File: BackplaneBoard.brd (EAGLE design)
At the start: 139.7 x 76.2 mm, 15 parts

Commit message: fixeey
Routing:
- net +3V3: track 127.7 -> 129.7 mm
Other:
- board text added: "+5V"
- board text added: "CAN"
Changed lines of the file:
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@@
 <?xml version="1.0" encoding="utf-8"?>
 <!DOCTYPE eagle SYSTEM "eagle.dtd">
-<eagle version="9.1.3">
+<eagle version="9.2.0">
 <drawing>
 <settings>
@@
 <wire x1="139.7" y1="76.2" x2="0" y2="76.2" width="0" layer="20"/>
 <wire x1="0" y1="76.2" x2="0" y2="0" width="0" layer="20"/>
+<text x="67.2338" y="71.628" size="1.778" layer="25">CAN</text>
+<text x="56.4134" y="2.1082" size="1.778" layer="25">+5V</text>
 </plain>
 <attributes>
@@
 <vertex x="134.1374" y="48.2346"/>
 <vertex x="134.1374" y="58.0898"/>
-<vertex x="133.9342" y="58.0898"/>
 <vertex x="122.7074" y="58.0898"/>
-<vertex x="122.7074" y="58.0136"/>
 <vertex x="122.7074" y="53.7718"/>
 <vertex x="122.7836" y="53.7718"/>
 <vertex x="120.2182" y="51.2064"/>
-<vertex x="27.3812" y="51.2064"/>
-<vertex x="17.5768" y="61.0108"/>
+<vertex x="25.019" y="51.2064"/>
+<vertex x="15.2146" y="61.0108"/>
 <vertex x="5.5626" y="61.0108"/>
 <vertex x="5.5626" y="50.6984"/>
@@
 <polygon width="0.1524" layer="1">
 <vertex x="35.56" y="20.32"/>
-<vertex x="35.56" y="26.67"/>
-<vertex x="33.02" y="29.21"/>
-<vertex x="27.94" y="29.21"/>
-<vertex x="26.2636" y="30.8864"/>
-<vertex x="26.2636" y="40.7416"/>
-<vertex x="26.2636" y="42.3164"/>
-<vertex x="22.86" y="45.72"/>
+<vertex x="35.56" y="26.3144"/>
+<vertex x="32.5628" y="29.3116"/>
+<vertex x="32.5628" y="41.4274"/>
+<vertex x="28.2702" y="45.72"/>
 <vertex x="21.59" y="45.72"/>
 <vertex x="16.4084" y="50.9016"/>
-<vertex x="16.4084" y="31.3944"/>
-<vertex x="23.5204" y="24.2824"/>
+<vertex x="16.4084" y="29.5656"/>
+<vertex x="23.5204" y="22.4536"/>
 <vertex x="23.5204" y="20.32"/>
+</polygon>
+<polygon width="0.1524" layer="1">
+<vertex x="12.0396" y="60.9854"/>
+<vertex x="24.8666" y="60.9854"/>
+<vertex x="24.8666" y="50.7746"/>
+<vertex x="12.0396" y="50.7746"/>
 </polygon>
 </signal>
@@
 <vertex x="6" y="28"/>
 </polygon>
-<wire x1="38.1" y1="16.51" x2="22.7584" y2="16.51" width="0.8128" layer="1"/>
+<wire x1="38.1" y1="16.51" x2="19.3548" y2="16.51" width="0.8128" layer="1"/>
 <polygon width="0.8128" layer="1">
 <vertex x="115.57" y="20.32"/>
@@
 <vertex x="120.65" y="20.32"/>
 </polygon>
-<wire x1="38.1" y1="16.51" x2="74.93" y2="16.51" width="0.8128" layer="1"/>
+<wire x1="38.1" y1="16.51" x2="76.2" y2="16.51" width="0.8128" layer="1"/>
 <wire x1="78.74" y1="21.59" x2="78.74" y2="19.05" width="0.8128" layer="1"/>
 <wire x1="78.74" y1="19.05" x2="76.2" y2="16.51" width="0.8128" layer="1"/>
-<wire x1="76.2" y1="16.51" x2="74.93" y2="16.51" width="0.8128" layer="1"/>
 <wire x1="40.64" y1="21.59" x2="40.64" y2="19.05" width="0.8128" layer="1"/>
 <wire x1="40.64" y1="19.05" x2="38.1" y2="16.51" width="0.8128" layer="1"/>
@@
 </polygon>
 <wire x1="116.84" y1="19.05" x2="116.84" y2="21.59" width="0.8128" layer="1"/>
-<wire x1="17.0688" y1="22.1996" x2="17.0688" y2="25.908" width="0.8128" layer="1"/>
-<wire x1="17.0688" y1="25.908" x2="13.7668" y2="29.21" width="0.8128" layer="1"/>
+<wire x1="16.0274" y1="26.9494" x2="16.0274" y2="19.8374" width="0.8128" layer="1"/>
+<wire x1="16.0274" y1="26.9494" x2="13.7668" y2="29.21" width="0.8128" layer="1"/>
 <wire x1="13.7668" y1="29.21" x2="12.4" y2="29.21" width="0.8128" layer="1"/>
-<wire x1="22.7584" y1="16.51" x2="17.0688" y2="22.1996" width="0.8128" layer="1"/>
+<wire x1="19.3548" y1="16.51" x2="16.0274" y2="19.8374" width="0.8128" layer="1"/>
 </signal>
 <signal name="CAN_H">

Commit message: Version #3
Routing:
- net CAN_L: track 286.2 -> 223.3 mm
- net CAN_H: track 183.3 -> 215.6 mm
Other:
- board text added: "+12V"
- board text added: "GND"

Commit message: Version 4
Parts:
- added U$12, U$13: T2I, BackplaneParts:T2I
- moved U$8 4.93 mm to (44.1, 5.92)
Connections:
- net +5V: now also U$12.1, U$12.2, U$12.3, U$12.4
- net GND: now also U$13.1, U$13.2, U$13.3, U$13.4
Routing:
- net +5V: track 97.9 -> 91.9 mm
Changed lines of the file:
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@@
 <wire x1="0" y1="76.2" x2="0" y2="0" width="0" layer="20"/>
 <text x="67.2338" y="71.628" size="1.778" layer="25">CAN</text>
-<text x="56.4134" y="2.1082" size="1.778" layer="25">+5V</text>
+<text x="51.7652" y="1.8796" size="1.778" layer="25">+5V</text>
 <text x="7.8232" y="62.5094" size="1.778" layer="25">+12V</text>
 <text x="7.493" y="12.065" size="1.778" layer="25">GND</text>
@@
 <text x="63.8048" y="44.2214" size="1.778" layer="25">+12V</text>
 <text x="25.5778" y="18.0086" size="1.778" layer="25">+12V</text>
+<text x="71.9582" y="2.286" size="1.778" layer="25">+5V</text>
+<text x="91.7194" y="2.413" size="1.778" layer="25">GND</text>
 </plain>
 <attributes>
@@
 <element name="U$6" library="BackplaneParts" package="T2I" value="T2I" x="45" y="42"/>
 <element name="U$7" library="BackplaneParts" package="T2I" value="T2I" x="87.988" y="70.636" rot="R180"/>
-<element name="U$8" library="BackplaneParts" package="T2I" value="T2I" x="49" y="6"/>
+<element name="U$8" library="BackplaneParts" package="T2I" value="T2I" x="44.0724" y="5.9238"/>
 <element name="U$9" library="BackplaneParts" package="T2I" value="T2I" x="27" y="42"/>
 <element name="U$10" library="BackplaneParts" package="T2I" value="T2I" x="45" y="31"/>
 <element name="U$11" library="BackplaneParts" package="T2I" value="T2I" x="27" y="31"/>
+<element name="U$12" library="BackplaneParts" package="T2I" value="T2I" x="63.754" y="5.8674"/>
+<element name="U$13" library="BackplaneParts" package="T2I" value="T2I" x="83.5406" y="6.1468"/>
 </elements>
 <signals>
@@
 <vertex x="139.7" y="76.2"/>
 </polygon>
+<contactref element="U$13" pad="1"/>
+<contactref element="U$13" pad="2"/>
+<contactref element="U$13" pad="3"/>
+<contactref element="U$13" pad="4"/>
 </signal>
 <signal name="+12V">
@@
 <contactref element="U$9" pad="1"/>
 <polygon width="0.2" layer="1">
-<vertex x="46" y="58"/>
-<vertex x="58" y="58"/>
+<vertex x="45.873" y="58.2794"/>
+<vertex x="58" y="58.2794"/>
 <vertex x="58" y="41"/>
-<vertex x="46" y="41"/>
+<vertex x="45.873" y="41"/>
 </polygon>
 <polygon width="0.1524" layer="1">
@@
 <vertex x="126.5428" y="40.64"/>
 <vertex x="134.1374" y="48.2346"/>
-<vertex x="134.1374" y="58.0898"/>
-<vertex x="122.7074" y="58.0898"/>
-<vertex x="122.7074" y="53.7718"/>
+<vertex x="134.1374" y="58.2676"/>
+<vertex x="122.3772" y="58.2676"/>
+<vertex x="122.3772" y="53.7718"/>
 <vertex x="122.7836" y="53.7718"/>
 <vertex x="120.2182" y="51.2064"/>
@@
 <contactref element="U$4" pad="P$G"/>
 <contactref element="U$4" pad="P$H"/>
+<polygon width="0.1524" layer="1">
+<vertex x="6" y="29"/>
+<vertex x="6" y="37"/>
+<vertex x="11" y="37"/>
+<vertex x="11" y="35"/>
+<vertex x="14" y="35"/>
+<vertex x="14" y="28"/>
+<vertex x="6" y="28"/>
+</polygon>
+<wire x1="38.1" y1="16.51" x2="19.3548" y2="16.51" width="0.8128" layer="1"/>
+<polygon width="0.8128" layer="1">
+<vertex x="115.57" y="20.32"/>
+<vertex x="115.57" y="25.4"/>
+<vertex x="120.65" y="20.32"/>
+</polygon>
+<wire x1="38.1" y1="16.51" x2="76.2" y2="16.51" width="0.8128" layer="1"/>
+<wire x1="78.74" y1="21.59" x2="78.74" y2="19.05" width="0.8128" layer="1"/>
+<wire x1="78.74" y1="19.05" x2="76.2" y2="16.51" width="0.8128" layer="1"/>
+<wire x1="40.64" y1="21.59" x2="40.64" y2="19.05" width="0.8128" layer="1"/>
+<wire x1="40.64" y1="19.05" x2="38.1" y2="16.51" width="0.8128" layer="1"/>
+<wire x1="76.2" y1="16.51" x2="114.3" y2="16.51" width="0.8128" layer="1"/>
+<wire x1="114.3" y1="16.51" x2="116.84" y2="19.05" width="0.8128" layer="1"/>
+<polygon width="0.1524" layer="1">
+<vertex x="39.37" y="20.32"/>
+<vertex x="39.37" y="25.4"/>
+<vertex x="44.45" y="25.4"/>
+<vertex x="44.45" y="20.32"/>
+</polygon>
+<polygon width="0.1524" layer="1">
+<vertex x="77.47" y="20.32"/>
+<vertex x="77.47" y="25.4"/>
+<vertex x="82.55" y="25.4"/>
+<vertex x="82.55" y="20.32"/>
+</polygon>
+<polygon width="0.1524" layer="1">
+<vertex x="115.57" y="20.32"/>
+<vertex x="115.57" y="25.4"/>
+<vertex x="120.65" y="25.4"/>
+<vertex x="120.65" y="20.32"/>
+</polygon>
+<wire x1="116.84" y1="19.05" x2="116.84" y2="21.59" width="0.8128" layer="1"/>
+<wire x1="16.0274" y1="19.8374" x2="16.0274" y2="26.9494" width="0.8128" layer="1"/>
+<wire x1="19.3548" y1="16.51" x2="16.0274" y2="19.8374" width="0.8128" layer="1"/>
+<contactref element="U$1" pad="17"/>
+<contactref element="U$1" pad="18"/>
+<contactref element="U$1" pad="19"/>
 <contactref element="U$1" pad="1"/>
 <contactref element="U$1" pad="4"/>
@@
 <contactref element="U$1" pad="11"/>
 <contactref element="U$1" pad="12"/>
-<contactref element="U$1" pad="17"/>
-<contactref element="U$1" pad="18"/>
-<contactref element="U$1" pad="19"/>
-<polygon width="0.1524" layer="1">
-<vertex x="6" y="29"/>
-<vertex x="6" y="37"/>
-<vertex x="11" y="37"/>
-<vertex x="11" y="35"/>
-<vertex x="14" y="35"/>
-<vertex x="14" y="28"/>
-<vertex x="6" y="28"/>
-</polygon>
-<wire x1="38.1" y1="16.51" x2="19.3548" y2="16.51" width="0.8128" layer="1"/>
-<polygon width="0.8128" layer="1">
-<vertex x="115.57" y="20.32"/>
-<vertex x="115.57" y="25.4"/>
-<vertex x="120.65" y="20.32"/>
-</polygon>
-<wire x1="38.1" y1="16.51" x2="76.2" y2="16.51" width="0.8128" layer="1"/>
-<wire x1="78.74" y1="21.59" x2="78.74" y2="19.05" width="0.8128" layer="1"/>
-<wire x1="78.74" y1="19.05" x2="76.2" y2="16.51" width="0.8128" layer="1"/>
-<wire x1="40.64" y1="21.59" x2="40.64" y2="19.05" width="0.8128" layer="1"/>
-<wire x1="40.64" y1="19.05" x2="38.1" y2="16.51" width="0.8128" layer="1"/>
-<wire x1="76.2" y1="16.51" x2="114.3" y2="16.51" width="0.8128" layer="1"/>
-<wire x1="114.3" y1="16.51" x2="116.84" y2="19.05" width="0.8128" layer="1"/>
-<polygon width="0.1524" layer="1">
-<vertex x="39.37" y="20.32"/>
-<vertex x="39.37" y="25.4"/>
-<vertex x="44.45" y="25.4"/>
-<vertex x="44.45" y="20.32"/>
-</polygon>
-<polygon width="0.1524" layer="1">
-<vertex x="77.47" y="20.32"/>
-<vertex x="77.47" y="25.4"/>
-<vertex x="82.55" y="25.4"/>
-<vertex x="82.55" y="20.32"/>
-</polygon>
-<polygon width="0.1524" layer="1">
-<vertex x="115.57" y="20.32"/>
-<vertex x="115.57" y="25.4"/>
-<vertex x="120.65" y="25.4"/>
-<vertex x="120.65" y="20.32"/>
-</polygon>
-<wire x1="116.84" y1="19.05" x2="116.84" y2="21.59" width="0.8128" layer="1"/>
-<wire x1="16.0274" y1="26.9494" x2="16.0274" y2="19.8374" width="0.8128" layer="1"/>
 <wire x1="16.0274" y1="26.9494" x2="13.7668" y2="29.21" width="0.8128" layer="1"/>
 <wire x1="13.7668" y1="29.21" x2="12.4" y2="29.21" width="0.8128" layer="1"/>
-<wire x1="19.3548" y1="16.51" x2="16.0274" y2="19.8374" width="0.8128" layer="1"/>
 </signal>
 <signal name="CAN_H">
@@
 </signal>
 <signal name="+5V">
-<contactref element="U$1" pad="13"/>
-<contactref element="U$1" pad="15"/>
-<contactref element="U$1" pad="16"/>
-<contactref element="U$1" pad="14"/>
+<contactref element="U$8" pad="4"/>
+<contactref element="U$8" pad="3"/>
+<contactref element="U$8" pad="2"/>
+<contactref element="U$8" pad="1"/>
+<polygon width="1.016" layer="1">
+<vertex x="43.3612" y="12"/>
+<vertex x="43.3612" y="5"/>
+<vertex x="82.1384" y="5"/>
+<vertex x="82.1384" y="12"/>
+</polygon>
+<wire x1="2" y1="10" x2="2" y2="39.13" width="1.27" layer="1"/>
+<wire x1="2" y1="10" x2="10" y2="2" width="1.27" layer="1"/>
+<polygon width="0.1524" layer="1">
+<vertex x="6.35" y="48.26"/>
+<vertex x="12.7" y="48.26"/>
+<vertex x="12.7" y="40.64"/>
+<vertex x="11.43" y="40.64"/>
+<vertex x="11.43" y="38.1"/>
+<vertex x="6.35" y="38.1"/>
+</polygon>
 <contactref element="U$1" pad="22"/>
 <contactref element="U$1" pad="23"/>
@@
 <contactref element="U$1" pad="7"/>
 <contactref element="U$1" pad="6"/>
-<contactref element="U$8" pad="4"/>
-<contactref element="U$8" pad="3"/>
-<contactref element="U$8" pad="2"/>
-<contactref element="U$8" pad="1"/>
-<polygon width="1.016" layer="1">
-<vertex x="49" y="12"/>
-<vertex x="49" y="5"/>
-<vertex x="67" y="5"/>
-<vertex x="67" y="12"/>
-</polygon>
-<wire x1="7.32" y1="44.45" x2="2" y2="39.13" width="1.27" layer="1"/>
-<wire x1="2" y1="39.13" x2="2" y2="10" width="1.27" layer="1"/>
-<wire x1="2" y1="10" x2="10" y2="2" width="1.27" layer="1"/>
-<wire x1="10" y1="2" x2="50" y2="2" width="1.27" layer="1"/>
-<wire x1="50" y1="2" x2="56.8" y2="8.8" width="1.27" layer="1"/>
-<wire x1="56.8" y1="8.8" x2="57.1" y2="8.8" width="1.27" layer="1"/>
-<polygon width="0.1524" layer="1">
-<vertex x="6.35" y="48.26"/>
-<vertex x="12.7" y="48.26"/>
-<vertex x="12.7" y="40.64"/>
-<vertex x="11.43" y="40.64"/>
-<vertex x="11.43" y="38.1"/>
-<vertex x="6.35" y="38.1"/>
-</polygon>
+<contactref element="U$1" pad="13"/>
+<contactref element="U$1" pad="15"/>
+<contactref element="U$1" pad="16"/>
+<contactref element="U$1" pad="14"/>
+<contactref element="U$12" pad="4"/>
+<contactref element="U$12" pad="3"/>
+<contactref element="U$12" pad="2"/>
+<contactref element="U$12" pad="1"/>
+<wire x1="10" y1="2" x2="45.4486" y2="2" width="1.27" layer="1"/>
+<wire x1="45.4486" y1="2" x2="52.1724" y2="8.7238" width="1.27" layer="1"/>
+<wire x1="2" y1="39.13" x2="2" y2="39.13" width="1.27" layer="1"/>
+<wire x1="2" y1="39.13" x2="4.78" y2="41.91" width="1.27" layer="1"/>
+<wire x1="4.78" y1="41.91" x2="7.32" y2="41.91" width="1.27" layer="1"/>
 </signal>
 </signals>

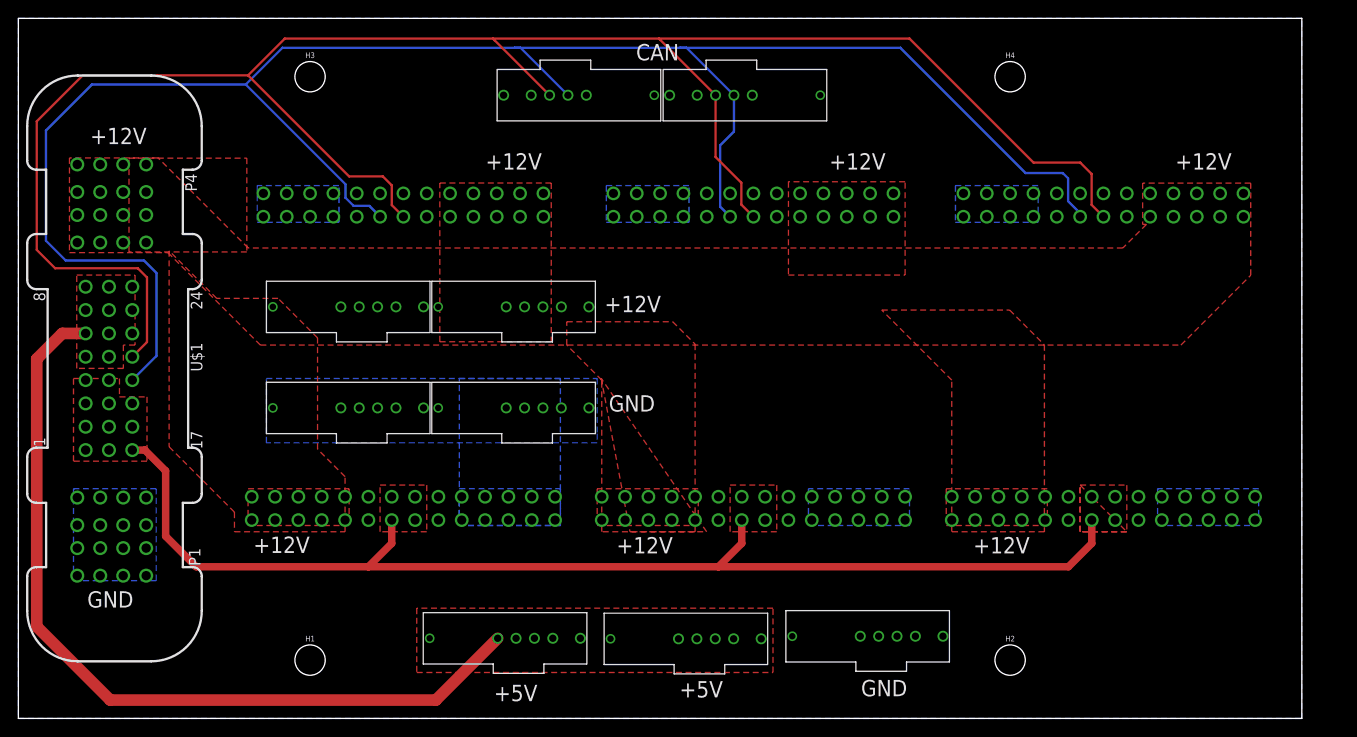
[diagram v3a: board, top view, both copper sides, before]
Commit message: edited GND plane
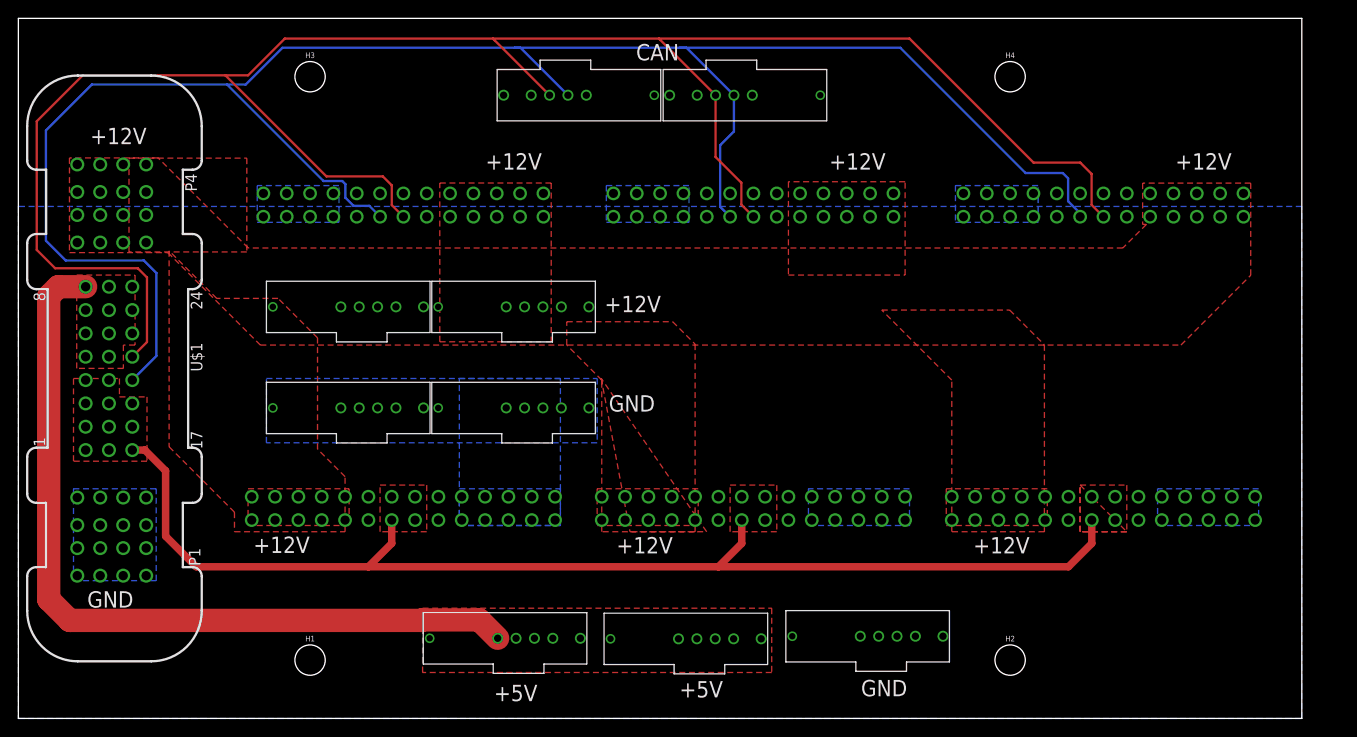
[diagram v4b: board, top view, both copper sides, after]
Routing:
- net CAN_L: track 223.3 -> 225.8 mm
- net CAN_H: track 215.6 -> 217.6 mm
- net +5V: track 91.9 -> 91.3 mm
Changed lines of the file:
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@@
 </polygon>
 <polygon width="0.8128" layer="16">
-<vertex x="0" y="76.2"/>
+<vertex x="0" y="55.7276"/>
 <vertex x="0" y="0"/>
 <vertex x="139.7" y="0"/>
-<vertex x="139.7" y="76.2"/>
+<vertex x="139.7" y="55.7276"/>
 </polygon>
 <contactref element="U$13" pad="1"/>
@@
 <wire x1="3" y1="52" x2="3" y2="64" width="0.254" layer="16"/>
 <wire x1="3" y1="64" x2="8" y2="69" width="0.254" layer="16"/>
-<wire x1="8" y1="69" x2="24.7498" y2="69" width="0.254" layer="16"/>
-<wire x1="24.7498" y1="69" x2="35.5974" y2="58.1524" width="0.254" layer="16"/>
+<wire x1="8" y1="69" x2="22.7076" y2="69" width="0.254" layer="16"/>
+<wire x1="22.7076" y1="69" x2="24.7498" y2="69" width="0.254" layer="16"/>
 <wire x1="35.5974" y1="58.1524" x2="35.5974" y2="56.6771625" width="0.254" layer="16"/>
 <wire x1="35.5974" y1="56.6771625" x2="36.4777625" y2="55.7968" width="0.254" layer="16"/>
@@
 <wire x1="24.7498" y1="69" x2="28.7498" y2="73" width="0.254" layer="16"/>
 <wire x1="28.7498" y1="73" x2="54" y2="73" width="0.254" layer="16"/>
+<wire x1="22.7076" y1="69" x2="33.2114" y2="58.4962" width="0.254" layer="16"/>
+<wire x1="35.2536" y1="58.4962" x2="35.5974" y2="58.1524" width="0.254" layer="16"/>
+<wire x1="33.2114" y1="58.4962" x2="35.2536" y2="58.4962" width="0.254" layer="16"/>
 </signal>
 <signal name="CAN_L">
@@
 <wire x1="51.656" y1="74" x2="51.828" y2="73.828" width="0.254" layer="1"/>
 <wire x1="51.828" y1="73.828" x2="57.82" y2="67.836" width="0.254" layer="1"/>
-<wire x1="7" y1="70" x2="25" y2="70" width="0.254" layer="1"/>
+<wire x1="7" y1="70" x2="22.5298" y2="70" width="0.254" layer="1"/>
+<wire x1="22.5298" y1="70" x2="25" y2="70" width="0.254" layer="1"/>
 <wire x1="51.656" y1="74" x2="69.724" y2="74" width="0.254" layer="1"/>
 <wire x1="69.724" y1="74" x2="69.862" y2="73.862" width="0.254" layer="1"/>
@@
 <wire x1="78.6952" y1="55.9248" x2="80.01" y2="54.61" width="0.254" layer="1"/>
 <wire x1="75.888" y1="61.112" x2="78.6952" y2="58.3048" width="0.254" layer="1"/>
-<wire x1="25" y1="70" x2="36" y2="59" width="0.254" layer="1"/>
-<wire x1="36" y1="59" x2="39.6698" y2="59" width="0.254" layer="1"/>
 <wire x1="39.6698" y1="59" x2="40.6444" y2="58.0254" width="0.254" layer="1"/>
 <wire x1="40.6444" y1="55.8756" x2="41.91" y2="54.61" width="0.254" layer="1"/>
 <wire x1="40.6444" y1="58.0254" x2="40.6444" y2="55.8756" width="0.254" layer="1"/>
+<wire x1="22.5298" y1="70" x2="33.5298" y2="59" width="0.254" layer="1"/>
+<wire x1="33.5298" y1="59" x2="39.6698" y2="59" width="0.254" layer="1"/>
 </signal>
 <signal name="+5V">
@@
 <contactref element="U$8" pad="2"/>
 <contactref element="U$8" pad="1"/>
-<polygon width="1.016" layer="1">
-<vertex x="43.3612" y="12"/>
-<vertex x="43.3612" y="5"/>
-<vertex x="82.1384" y="5"/>
-<vertex x="82.1384" y="12"/>
-</polygon>
-<wire x1="2" y1="10" x2="2" y2="39.13" width="1.27" layer="1"/>
-<wire x1="2" y1="10" x2="10" y2="2" width="1.27" layer="1"/>
 <polygon width="0.1524" layer="1">
 <vertex x="6.35" y="48.26"/>
@@
 <contactref element="U$12" pad="2"/>
 <contactref element="U$12" pad="1"/>
-<wire x1="10" y1="2" x2="45.4486" y2="2" width="1.27" layer="1"/>
-<wire x1="45.4486" y1="2" x2="52.1724" y2="8.7238" width="1.27" layer="1"/>
-<wire x1="2" y1="39.13" x2="2" y2="39.13" width="1.27" layer="1"/>
-<wire x1="2" y1="39.13" x2="4.78" y2="41.91" width="1.27" layer="1"/>
-<wire x1="4.78" y1="41.91" x2="7.32" y2="41.91" width="1.27" layer="1"/>
+<polygon width="0.1524" layer="1">
+<vertex x="44" y="5"/>
+<vertex x="44" y="12"/>
+<vertex x="82" y="12"/>
+<vertex x="82" y="5"/>
+</polygon>
+<wire x1="49.8962" y1="11" x2="52.1724" y2="8.7238" width="1.27" layer="1"/>
+<wire x1="7.32" y1="46.99" x2="4.3434" y2="46.99" width="2.54" layer="1"/>
+<wire x1="4.3434" y1="46.99" x2="3.302" y2="45.9486" width="2.54" layer="1"/>
+<wire x1="3.302" y1="45.9486" x2="3.302" y2="12.954" width="2.54" layer="1"/>
+<wire x1="3.302" y1="12.954" x2="5.588" y2="10.668" width="2.54" layer="1"/>
+<wire x1="5.588" y1="10.668" x2="43.88675625" y2="10.668" width="2.54" layer="1"/>
+<wire x1="43.88675625" y1="10.668" x2="43.94355625" y2="10.7248" width="2.54" layer="1"/>
+<wire x1="43.94355625" y1="10.7248" x2="50.1714" y2="10.7248" width="2.54" layer="1"/>
+<wire x1="50.1714" y1="10.7248" x2="52.1724" y2="8.7238" width="2.54" layer="1"/>
 </signal>
 </signals>
